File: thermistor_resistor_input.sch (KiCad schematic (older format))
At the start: 4 parts, among them P39 CONN_1, P40 CONN_1, Q10 MOS_N

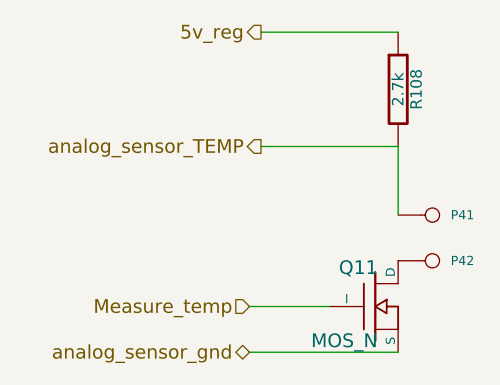
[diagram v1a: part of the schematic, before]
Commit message: Exchanged current sensing with peak&hold, and a closer approach to a more integrated design.
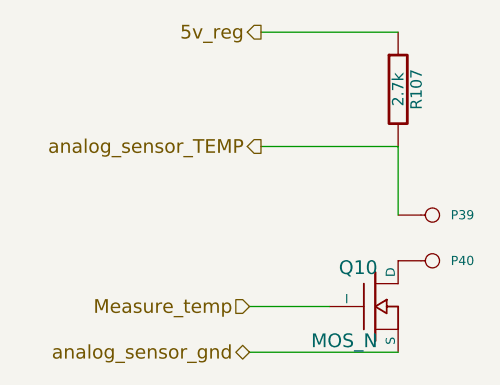
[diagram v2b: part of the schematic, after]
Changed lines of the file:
@@
-EESchema Schematic File Version 2  date Sat 03 Jul 2010 05:37:07 PM ART
+EESchema Schematic File Version 2  date Thu 22 Jul 2010 10:06:33 AM ART
 LIBS:power
 LIBS:freeEMS_lib
@@
 EELAYER END
 $Descr A 11000 8500
-Sheet 39 41
+Sheet 40 41
 Title "freeEMS 1.0"
-Date "3 jul 2010"
+Date "22 jul 2010"
 Rev "A.07"
 Comp "diyefi.org"
@@
 AR Path="/4C2E1E9D/4C2F5338" Ref="Q10"  Part="1"
 AR Path="/4C2E1E9F/4C2F5338" Ref="Q11"  Part="1"
-F 0 "Q11" H 3210 2320 60  0000 R CNN
+F 0 "Q10" H 3210 2320 60  0000 R CNN
 F 1 "MOS_N" H 3210 2000 60  0000 R CNN
 F 2 "TO92" V 3130 2900 60  0001 C CNN
@@
 AR Path="/4C2E1E9D/48AA1AB3" Ref="P40"  Part="1"
 AR Path="/4C2E1E9F/48AA1AB3" Ref="P42"  Part="1"
-F 0 "P42" H 3530 1950 40  0000 L CNN
+F 0 "P40" H 3530 1950 40  0000 L CNN
 F 1 "CONN_1" H 3450 2005 30  0001 C CNN
 F 2 "1PIN" V 1130 2600 60  0001 C CNN
@@
 AR Path="/4C2E1E9D/48AA1AB0" Ref="P39"  Part="1"
 AR Path="/4C2E1E9F/48AA1AB0" Ref="P41"  Part="1"
-F 0 "P41" H 3530 1750 40  0000 L CNN
+F 0 "P39" H 3530 1750 40  0000 L CNN
 F 1 "CONN_1" H 3450 1805 30  0001 C CNN
 F 2 "1PIN" V 1130 2600 60  0001 C CNN
@@
 AR Path="/4C2E1E9D/488E4A25" Ref="R107"  Part="1"
 AR Path="/4C2E1E9F/488E4A25" Ref="R108"  Part="1"
-F 0 "R108" V 3380 1200 50  0000 C CNN
+F 0 "R107" V 3380 1200 50  0000 C CNN
 F 1 "2.7k" V 3300 1200 50  0000 C CNN
 F 2 "R4-SM0805" V 3480 1300 60  0001 C CNN

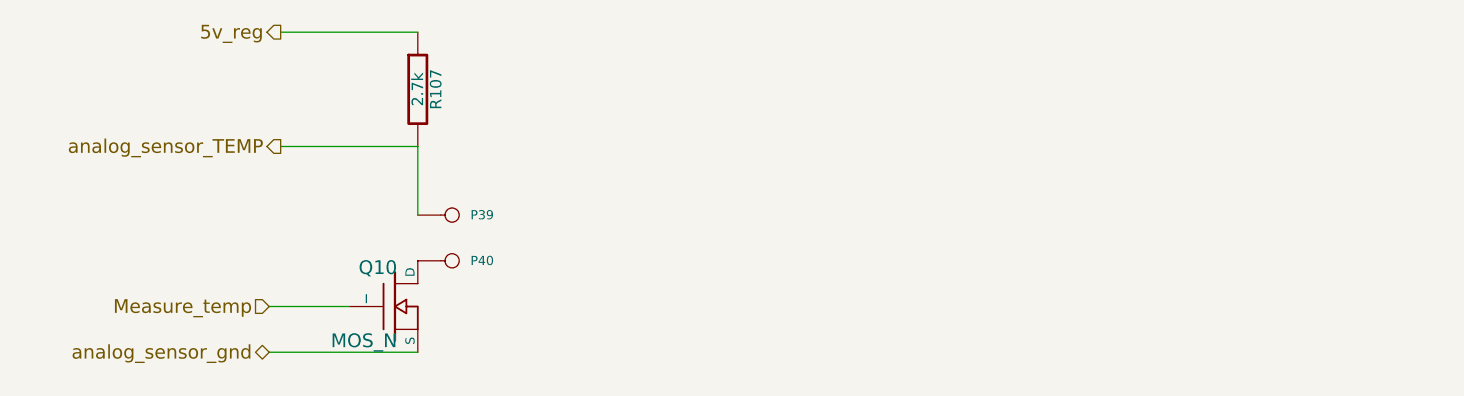
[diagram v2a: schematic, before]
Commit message: MAP circuit compatible with external sensors. Baro is left untouched
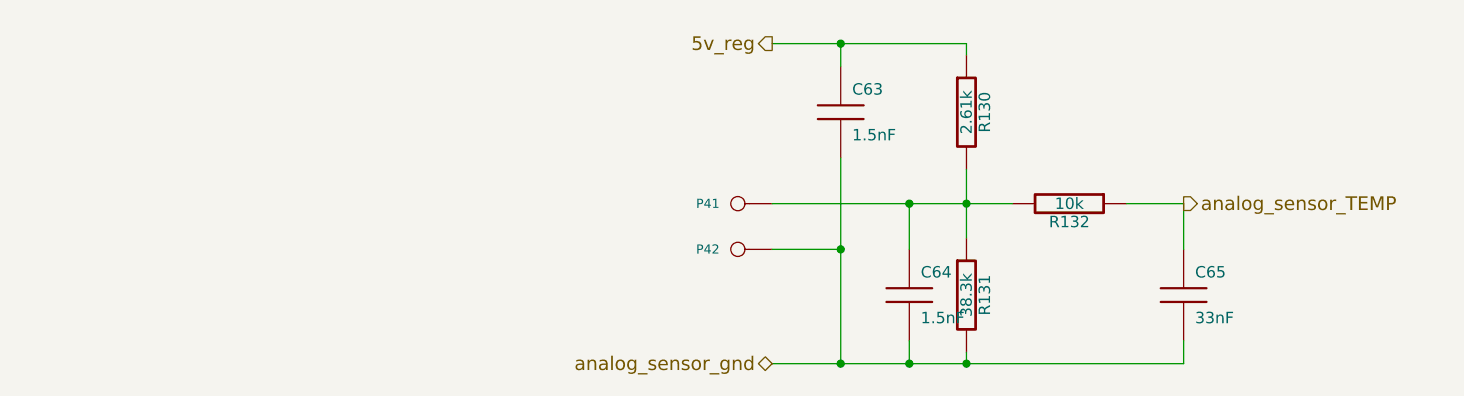
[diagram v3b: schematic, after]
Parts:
- removed Q10: MOS_N, TO92, symbol PIP-3104
- removed R107: 2.7k, R4-SM0805, symbol R
- added C63, C64: 1.5nF, symbol C
- added C65: 33nF, symbol C
- added R130: 2.61k, symbol R
- added R131: 38.3k, symbol R
- added R132: 10k, symbol R
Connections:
- net 5v_reg: now also C63.1, R130.1
- net analog_sensor_TEMP: now also C65.1, R132.1; no longer P39.1
- net analog_sensor_gnd: now also P40.1, C63.2, C64.2, C65.2, R131.2
- new net: C64.1, P39.1, R130.2, R131.1, R132.2
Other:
- moved on the sheet: P41, P42
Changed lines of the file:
@@
-EESchema Schematic File Version 2  date Thu 22 Jul 2010 10:06:33 AM ART
+EESchema Schematic File Version 2  date Sat 24 Jul 2010 11:01:40 AM ART
 LIBS:power
 LIBS:freeEMS_lib
@@
 EELAYER END
 $Descr A 11000 8500
-Sheet 40 41
+Sheet 39 41
 Title "freeEMS 1.0"
-Date "22 jul 2010"
+Date "24 jul 2010"
 Rev "A.07"
 Comp "diyefi.org"
@@
 Comment4 ""
 $EndDescr
+Connection ~ 5150 1900
+Wire Wire Line
+	4850 1900 5150 1900
+Connection ~ 5150 1000
+Wire Wire Line
+	4850 1000 5700 1000
+Connection ~ 5450 2400
+Wire Wire Line
+	5150 2400 5150 1500
+Wire Wire Line
+	4850 1700 5900 1700
+Wire Wire Line
+	5700 1000 5700 1050
+Wire Wire Line
+	5150 1000 5150 1100
+Connection ~ 5700 1700
+Wire Wire Line
+	5700 1850 5700 1550
+Wire Wire Line
+	6650 1900 6650 1700
+Wire Wire Line
+	6650 1700 6400 1700
+Wire Wire Line
+	5700 2400 5700 2350
+Wire Wire Line
+	5450 2400 5450 2300
+Wire Wire Line
+	5450 1900 5450 1700
+Connection ~ 5450 1700
+Wire Wire Line
+	6650 2300 6650 2400
+Connection ~ 5700 2400
+Wire Wire Line
+	6650 2400 4850 2400
+Connection ~ 5150 2400
 $Comp
-L PIP-3104 Q10
-U 1 1 4C2F5338
-P 3200 2150
-AR Path="/4C2E1E9D/4C2F5338" Ref="Q10"  Part="1"
-AR Path="/4C2E1E9F/4C2F5338" Ref="Q11"  Part="1"
-F 0 "Q10" H 3210 2320 60  0000 R CNN
-F 1 "MOS_N" H 3210 2000 60  0000 R CNN
-F 2 "TO92" V 3130 2900 60  0001 C CNN
-F 4 "digi,PIP3104-ND" V 1330 3900 60  0001 C CNN "Field1"
-F 5 "vendor1, smd w hem" V 1330 3900 60  0001 C CNN "Field2"
-F 6 "vendor2, thru w hem" V 1330 3900 60  0001 C CNN "Field3"
-F 7 "vendor2, smd w hem" V 1330 3900 60  0001 C CNN "Field4"
-F 8 "8,A" V 1330 3900 60  0001 C CNN "Field5"
-F 9 "x,x" V 1330 3900 60  0001 C CNN "Field6"
-F 10 "TOPFET" V 1330 3900 60  0001 C CNN "Field7"
-F 11 "other,more,stuff" V 1330 3900 60  0001 C CNN "Field8"
-	1    3200 2150
+L C C65
+U 1 1 4C4AE9AE
+P 6650 2100
+AR Path="/4C2E1E9F/4C4AE9AE" Ref="C65"  Part="1"
+AR Path="/4C2E1E9D/4C4AE9AE" Ref="C62"  Part="1"
+F 0 "C65" H 6700 2200 50  0000 L CNN
+F 1 "33nF" H 6700 2000 50  0000 L CNN
+	1    6650 2100
+	1    0    0    -1
+$EndComp
+$Comp
+L C C64
+U 1 1 4C4AE9A4
+P 5450 2100
+AR Path="/4C2E1E9F/4C4AE9A4" Ref="C64"  Part="1"
+AR Path="/4C2E1E9D/4C4AE9A4" Ref="C61"  Part="1"
+F 0 "C64" H 5500 2200 50  0000 L CNN
+F 1 "1.5nF" H 5500 2000 50  0000 L CNN
+	1    5450 2100
+	1    0    0    -1
+$EndComp
+$Comp
+L C C63
+U 1 1 4C4AE98C
+P 5150 1300
+AR Path="/4C2E1E9F/4C4AE98C" Ref="C63"  Part="1"
+AR Path="/4C2E1E9D/4C4AE98C" Ref="C60"  Part="1"
+F 0 "C63" H 5200 1400 50  0000 L CNN
+F 1 "1.5nF" H 5200 1200 50  0000 L CNN
+	1    5150 1300
+	1    0    0    -1
+$EndComp
+$Comp
+L R R132
+U 1 1 4C4AE957
+P 6150 1700
+AR Path="/4C2E1E9F/4C4AE957" Ref="R132"  Part="1"
+AR Path="/4C2E1E9D/4C4AE957" Ref="R129"  Part="1"
+F 0 "R132" V 6230 1700 50  0000 C CNN
+F 1 "10k" V 6150 1700 50  0000 C CNN
+	1    6150 1700
+	0    1    1    0
+$EndComp
+$Comp
+L R R131
+U 1 1 4C4AE952
+P 5700 2100
+AR Path="/4C2E1E9F/4C4AE952" Ref="R131"  Part="1"
+AR Path="/4C2E1E9D/4C4AE952" Ref="R128"  Part="1"
+F 0 "R131" V 5780 2100 50  0000 C CNN
+F 1 "38.3k" V 5700 2100 50  0000 C CNN
+	1    5700 2100
+	1    0    0    -1
+$EndComp
+$Comp
+L R R130
+U 1 1 4C4AE94D
+P 5700 1300
+AR Path="/4C2E1E9F/4C4AE94D" Ref="R130"  Part="1"
+AR Path="/4C2E1E9D/4C4AE94D" Ref="R127"  Part="1"
+F 0 "R130" V 5780 1300 50  0000 C CNN
+F 1 "2.61k" V 5700 1300 50  0000 C CNN
+	1    5700 1300
 	1    0    0    -1
 $EndComp
@@
 L CONN_1 P40
 U 1 1 48AA1AB3
-P 3450 1950
+P 4700 1900
 AR Path="/4C2E1E9D/48AA1AB3" Ref="P40"  Part="1"
 AR Path="/4C2E1E9F/48AA1AB3" Ref="P42"  Part="1"
-F 0 "P40" H 3530 1950 40  0000 L CNN
-F 1 "CONN_1" H 3450 2005 30  0001 C CNN
-F 2 "1PIN" V 1130 2600 60  0001 C CNN
-	1    3450 1950
-	1    0    0    -1
+F 0 "P42" H 4780 1900 40  0000 L CNN
+F 1 "CONN_1" H 4700 1955 30  0001 C CNN
+F 2 "1PIN" V 2380 2550 60  0001 C CNN
+	1    4700 1900
+	-1   0    0    1
 $EndComp
 $Comp
 L CONN_1 P39
 U 1 1 48AA1AB0
-P 3450 1750
+P 4700 1700
 AR Path="/4C2E1E9D/48AA1AB0" Ref="P39"  Part="1"
 AR Path="/4C2E1E9F/48AA1AB0" Ref="P41"  Part="1"
-F 0 "P39" H 3530 1750 40  0000 L CNN
-F 1 "CONN_1" H 3450 1805 30  0001 C CNN
-F 2 "1PIN" V 1130 2600 60  0001 C CNN
-	1    3450 1750
-	1    0    0    -1
+F 0 "P41" H 4780 1700 40  0000 L CNN
+F 1 "CONN_1" H 4700 1755 30  0001 C CNN
+F 2 "1PIN" V 2380 2550 60  0001 C CNN
+	1    4700 1700
+	-1   0    0    1
 $EndComp
-Wire Wire Line
-	3300 1750 3300 1450
-Wire Wire Line
-	2650 2150 3000 2150
-Wire Wire Line
-	2700 950  3300 950
-Wire Wire Line
-	3300 1450 2700 1450
-Wire Wire Line
-	2650 2350 3300 2350
-Text HLabel 2700 950  0    60   Output ~ 0
+Text HLabel 4850 1000 0    60   Output ~ 0
 5v_reg
-$Comp
-L R R107
-U 1 1 488E4A25
-P 3300 1200
-AR Path="/4C2E1E9D/488E4A25" Ref="R107"  Part="1"
-AR Path="/4C2E1E9F/488E4A25" Ref="R108"  Part="1"
-F 0 "R107" V 3380 1200 50  0000 C CNN
-F 1 "2.7k" V 3300 1200 50  0000 C CNN
-F 2 "R4-SM0805" V 3480 1300 60  0001 C CNN
-F 4 "newark,41K8850" V 1130 2600 60  0001 C CNN "Field1"
-F 5 "vendor1, smd w hem" V 1130 2600 60  0001 C CNN "Field2"
-F 6 "vendor2, thru w hem" V 1130 2600 60  0001 C CNN "Field3"
-F 7 "vendor2, smd w hem" V 1130 2600 60  0001 C CNN "Field4"
-F 8 ".5,W" V 1130 2600 60  0001 C CNN "Field5"
-F 9 "1,%" V 1130 2600 60  0001 C CNN "Field6"
-F 10 "metal film" V 1130 2600 60  0001 C CNN "Field7"
-F 11 "other,more,stuff" V 1130 2600 60  0001 C CNN "Field8"
-	1    3300 1200
-	1    0    0    -1
-$EndComp
-Text HLabel 2650 2150 0    60   Input ~ 0
-Measure_temp
-Text HLabel 2650 2350 0    60   BiDi ~ 0
+Text HLabel 4850 2400 0    60   BiDi ~ 0
 analog_sensor_gnd
-Text HLabel 2700 1450 0    60   Output ~ 0
+Text HLabel 6650 1700 2    60   Output ~ 0
 analog_sensor_TEMP
 $EndSCHEMATC

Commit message: 4 temperature inputs and 2 extra aux analog inputs.
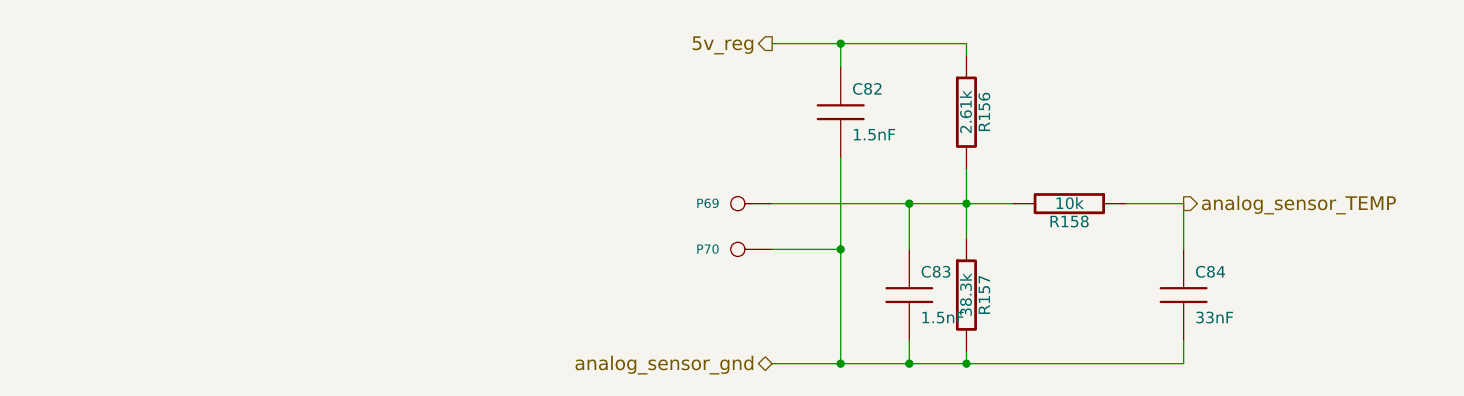
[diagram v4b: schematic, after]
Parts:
- renumbered C63 to C82, C64 to C83, C65 to C84, P39 to P69, P40 to P70, R130 to R156, R131 to R157, R132 to R158
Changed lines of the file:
@@
-EESchema Schematic File Version 2  date Sat 24 Jul 2010 11:01:40 AM ART
+EESchema Schematic File Version 2  date Sun 25 Jul 2010 03:39:31 PM ART
 LIBS:power
 LIBS:freeEMS_lib
@@
 EELAYER END
 $Descr A 11000 8500
-Sheet 39 41
+Sheet 6 46
 Title "freeEMS 1.0"
-Date "24 jul 2010"
+Date "25 jul 2010"
 Rev "A.07"
 Comp "diyefi.org"
@@
 Connection ~ 5150 2400
 $Comp
-L C C65
+L C C84
 U 1 1 4C4AE9AE
 P 6650 2100
-AR Path="/4C2E1E9F/4C4AE9AE" Ref="C65"  Part="1"
-AR Path="/4C2E1E9D/4C4AE9AE" Ref="C62"  Part="1"
-F 0 "C65" H 6700 2200 50  0000 L CNN
+AR Path="/4C4C62BF/4C4AE9AE" Ref="C84"  Part="1"
+AR Path="/4C4C628B/4C4AE9AE" Ref="C81"  Part="1"
+AR Path="/4C2E1E9D/4C4AE9AE" Ref="C75"  Part="1"
+AR Path="/4C2E1E9F/4C4AE9AE" Ref="C78"  Part="1"
+F 0 "C84" H 6700 2200 50  0000 L CNN
 F 1 "33nF" H 6700 2000 50  0000 L CNN
 	1    6650 2100
@@
 $EndComp
 $Comp
-L C C64
+L C C83
 U 1 1 4C4AE9A4
 P 5450 2100
-AR Path="/4C2E1E9F/4C4AE9A4" Ref="C64"  Part="1"
-AR Path="/4C2E1E9D/4C4AE9A4" Ref="C61"  Part="1"
-F 0 "C64" H 5500 2200 50  0000 L CNN
+AR Path="/4C4C62BF/4C4AE9A4" Ref="C83"  Part="1"
+AR Path="/4C4C628B/4C4AE9A4" Ref="C80"  Part="1"
+AR Path="/4C2E1E9D/4C4AE9A4" Ref="C74"  Part="1"
+AR Path="/4C2E1E9F/4C4AE9A4" Ref="C77"  Part="1"
+F 0 "C83" H 5500 2200 50  0000 L CNN
 F 1 "1.5nF" H 5500 2000 50  0000 L CNN
 	1    5450 2100
@@
 $EndComp
 $Comp
-L C C63
+L C C82
 U 1 1 4C4AE98C
 P 5150 1300
-AR Path="/4C2E1E9F/4C4AE98C" Ref="C63"  Part="1"
-AR Path="/4C2E1E9D/4C4AE98C" Ref="C60"  Part="1"
-F 0 "C63" H 5200 1400 50  0000 L CNN
+AR Path="/4C4C62BF/4C4AE98C" Ref="C82"  Part="1"
+AR Path="/4C4C628B/4C4AE98C" Ref="C79"  Part="1"
+AR Path="/4C2E1E9D/4C4AE98C" Ref="C73"  Part="1"
+AR Path="/4C2E1E9F/4C4AE98C" Ref="C76"  Part="1"
+F 0 "C82" H 5200 1400 50  0000 L CNN
 F 1 "1.5nF" H 5200 1200 50  0000 L CNN
 	1    5150 1300
@@
 $EndComp
 $Comp
-L R R132
+L R R158
 U 1 1 4C4AE957
 P 6150 1700
-AR Path="/4C2E1E9F/4C4AE957" Ref="R132"  Part="1"
-AR Path="/4C2E1E9D/4C4AE957" Ref="R129"  Part="1"
-F 0 "R132" V 6230 1700 50  0000 C CNN
+AR Path="/4C4C62BF/4C4AE957" Ref="R158"  Part="1"
+AR Path="/4C4C628B/4C4AE957" Ref="R155"  Part="1"
+AR Path="/4C2E1E9D/4C4AE957" Ref="R149"  Part="1"
+AR Path="/4C2E1E9F/4C4AE957" Ref="R152"  Part="1"
+F 0 "R158" V 6230 1700 50  0000 C CNN
 F 1 "10k" V 6150 1700 50  0000 C CNN
 	1    6150 1700
@@
 $EndComp
 $Comp
-L R R131
+L R R157
 U 1 1 4C4AE952
 P 5700 2100
-AR Path="/4C2E1E9F/4C4AE952" Ref="R131"  Part="1"
-AR Path="/4C2E1E9D/4C4AE952" Ref="R128"  Part="1"
-F 0 "R131" V 5780 2100 50  0000 C CNN
+AR Path="/4C4C62BF/4C4AE952" Ref="R157"  Part="1"
+AR Path="/4C4C628B/4C4AE952" Ref="R154"  Part="1"
+AR Path="/4C2E1E9D/4C4AE952" Ref="R148"  Part="1"
+AR Path="/4C2E1E9F/4C4AE952" Ref="R151"  Part="1"
+F 0 "R157" V 5780 2100 50  0000 C CNN
 F 1 "38.3k" V 5700 2100 50  0000 C CNN
 	1    5700 2100
@@
 $EndComp
 $Comp
-L R R130
+L R R156
 U 1 1 4C4AE94D
 P 5700 1300
-AR Path="/4C2E1E9F/4C4AE94D" Ref="R130"  Part="1"
-AR Path="/4C2E1E9D/4C4AE94D" Ref="R127"  Part="1"
-F 0 "R130" V 5780 1300 50  0000 C CNN
+AR Path="/4C4C62BF/4C4AE94D" Ref="R156"  Part="1"
+AR Path="/4C4C628B/4C4AE94D" Ref="R153"  Part="1"
+AR Path="/4C2E1E9D/4C4AE94D" Ref="R147"  Part="1"
+AR Path="/4C2E1E9F/4C4AE94D" Ref="R150"  Part="1"
+F 0 "R156" V 5780 1300 50  0000 C CNN
 F 1 "2.61k" V 5700 1300 50  0000 C CNN
 	1    5700 1300
@@
 $EndComp
 $Comp
-L CONN_1 P40
+L CONN_1 P70
 U 1 1 48AA1AB3
 P 4700 1900
-AR Path="/4C2E1E9D/48AA1AB3" Ref="P40"  Part="1"
-AR Path="/4C2E1E9F/48AA1AB3" Ref="P42"  Part="1"
-F 0 "P42" H 4780 1900 40  0000 L CNN
+AR Path="/4C4C62BF/48AA1AB3" Ref="P70"  Part="1"
+AR Path="/4C4C628B/48AA1AB3" Ref="P68"  Part="1"
+AR Path="/4C2E1E9D/48AA1AB3" Ref="P64"  Part="1"
+AR Path="/4C2E1E9F/48AA1AB3" Ref="P66"  Part="1"
+F 0 "P70" H 4780 1900 40  0000 L CNN
 F 1 "CONN_1" H 4700 1955 30  0001 C CNN
 F 2 "1PIN" V 2380 2550 60  0001 C CNN
@@
 $EndComp
 $Comp
-L CONN_1 P39
+L CONN_1 P69
 U 1 1 48AA1AB0
 P 4700 1700
-AR Path="/4C2E1E9D/48AA1AB0" Ref="P39"  Part="1"
-AR Path="/4C2E1E9F/48AA1AB0" Ref="P41"  Part="1"
-F 0 "P41" H 4780 1700 40  0000 L CNN
+AR Path="/4C4C62BF/48AA1AB0" Ref="P69"  Part="1"
+AR Path="/4C4C628B/48AA1AB0" Ref="P67"  Part="1"
+AR Path="/4C2E1E9D/48AA1AB0" Ref="P63"  Part="1"
+AR Path="/4C2E1E9F/48AA1AB0" Ref="P65"  Part="1"
+F 0 "P69" H 4780 1700 40  0000 L CNN
 F 1 "CONN_1" H 4700 1755 30  0001 C CNN
 F 2 "1PIN" V 2380 2550 60  0001 C CNN
